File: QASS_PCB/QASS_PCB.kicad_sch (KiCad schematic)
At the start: 89 parts, among them U2 Seeeduino Xiao rp2040

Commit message: working on it
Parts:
- removed D1, D10, D11, D12, D13, D14, D15, D16, D17, D18, D19, D2, D20, D21, D22, D23, D24, D25, D26, D27, D28, D29, D3, D30, D31, D32, D33, D34, D35, D36, D37, D38, D39, D4, D5, D6, D7, D8, D9: D_Small, Diode_SMD:D_SOD-123, symbol Device:D_Small
- removed U2: Seeeduino Xiao rp2040, PCM_marbastlib-xp-promicroish:Xiao_rp2040_ACH, symbol PCM_marbastlib-promicroish:Seeeduino_Xiao_rp2040
- added D1, D10, D11, D12, D13, D14, D15, D16, D17, D18, D19, D2, D3, D4, D40, D5, D6, D7, D8, D9: BAV70_Small, Package_TO_SOT_SMD:SOT-23, symbol PCM_marbastlib-various:BAV70_Small
- added J1: Conn_01x02_Pin, Connector_PinHeader_2.54mm:PinHeader_1x02_P2.54mm_Vertical, symbol Connector:Conn_01x02_Pin
- added U1: ~, Einzelne Custom:Miao, symbol Miao:Miao_full_pinout
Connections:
- net c10 is gone; now on net c9: MX11.1
- net c1: now also MX13.2, MX2.2, MX23.2; no longer MX13.1, MX2.1, MX23.1
- net c2: now also MX33.2; no longer MX33.1
- net c3: now also MX15.2, MX25.2, MX4.2; no longer MX15.1, MX25.1, MX4.1
- net c4: now also MX35.2, MX40.2; no longer MX35.1, MX41.1
- net c5: now also MX17.2, MX27.2, MX41.1, MX6.2; no longer MX17.1, MX27.1, MX6.1
- net c6: now also MX37.2; no longer MX37.1, MX40.1
- net c7: now also MX19.2, MX29.2, MX8.2; no longer MX19.1, MX29.1, MX8.1
- net c8: now also MX39.2; no longer MX39.1
- net c9: now also MX10.2, MX21.2, MX31.2; no longer MX10.1, MX21.1, MX31.1
- net r0: now also D1.3 (K), D2.3 (K), D3.3 (K), D4.3 (K), D40.3 (K)
- net r1: now also D5.3 (K), D6.3 (K), D7.3 (K), D8.3 (K), D9.3 (K)
- net r2: now also D10.3 (K), D11.3 (K), D12.3 (K), D13.3 (K), D14.3 (K)
- net r3: now also D15.3 (K), D16.3 (K), D17.3 (K), D18.3 (K), D19.3 (K)
- net at MX14.2: now also D6.1 (A1)
- net at MX38.2: now also D18.1 (A1)
- net at MX30.2: now also D14.1 (A1)
- net at MX22.2: now also D10.1 (A1)
- net at MX41.2: now also MX36.2, MX42.2, D17.1 (A1); no longer MX35.2
- net at MX18.2: now also D8.1 (A1)
- net at MX28.2: now also D13.1 (A1)
- net at MX20.2: now also D9.1 (A1)
- net at MX7.2: now also D3.1 (A1)
- net at MX9.2: now also D4.1 (A1)
- net at MX24.2: now also D11.1 (A1)
- net at MX32.2: now also D15.1 (A1)
- net at MX26.2: now also D12.1 (A1)
- net at MX12.2: now also D5.1 (A1)
- net at MX16.2: now also D7.1 (A1)
- net at MX5.2: now also D2.1 (A1)
- net at MX11.2: now also D19.2 (A2)
- net at MX3.2: now also D1.1 (A1)
- net at MX1.2: now also D40.1 (A1)
- net at MX34.2: now also D16.1 (A1)
- new net: D7.2 (A2), MX17.1
- new net: D11.2 (A2), MX25.1
- new net: D40.2 (A2), MX2.1
- new net: D16.2 (A2), MX35.1, MX40.1
- new net: D4.2 (A2), MX10.1
- new net: D3.2 (A2), MX8.1
- new net: D18.2 (A2), MX39.1
- new net: D10.2 (A2), MX23.1
- new net: D5.2 (A2), MX13.1
- new net: D15.2 (A2), MX33.1
- new net: D6.2 (A2), MX15.1
- new net: D8.2 (A2), MX19.1
- new net: D17.2 (A2), MX37.1
- new net: D2.2 (A2), MX6.1
- new net: D1.2 (A2), MX4.1
- new net: D12.2 (A2), MX27.1
- new net: D13.2 (A2), MX29.1
- new net: D9.2 (A2), MX21.1
- new net: D14.2 (A2), MX31.1
- no-connect marks 0 -> 2
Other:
- note added: "L_Mods"
- note added: "R_Mods"
- note added: "Spacebars 2u"
- note added: "Spacebars 3u"
- note added: "Spacebars long"
- note added: "Xiao-compatibility for pads on backside"
- moved on the sheet: MX1, MX10, MX11, MX12, MX13, MX14, MX15, MX16, MX17, MX18, MX19, MX2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

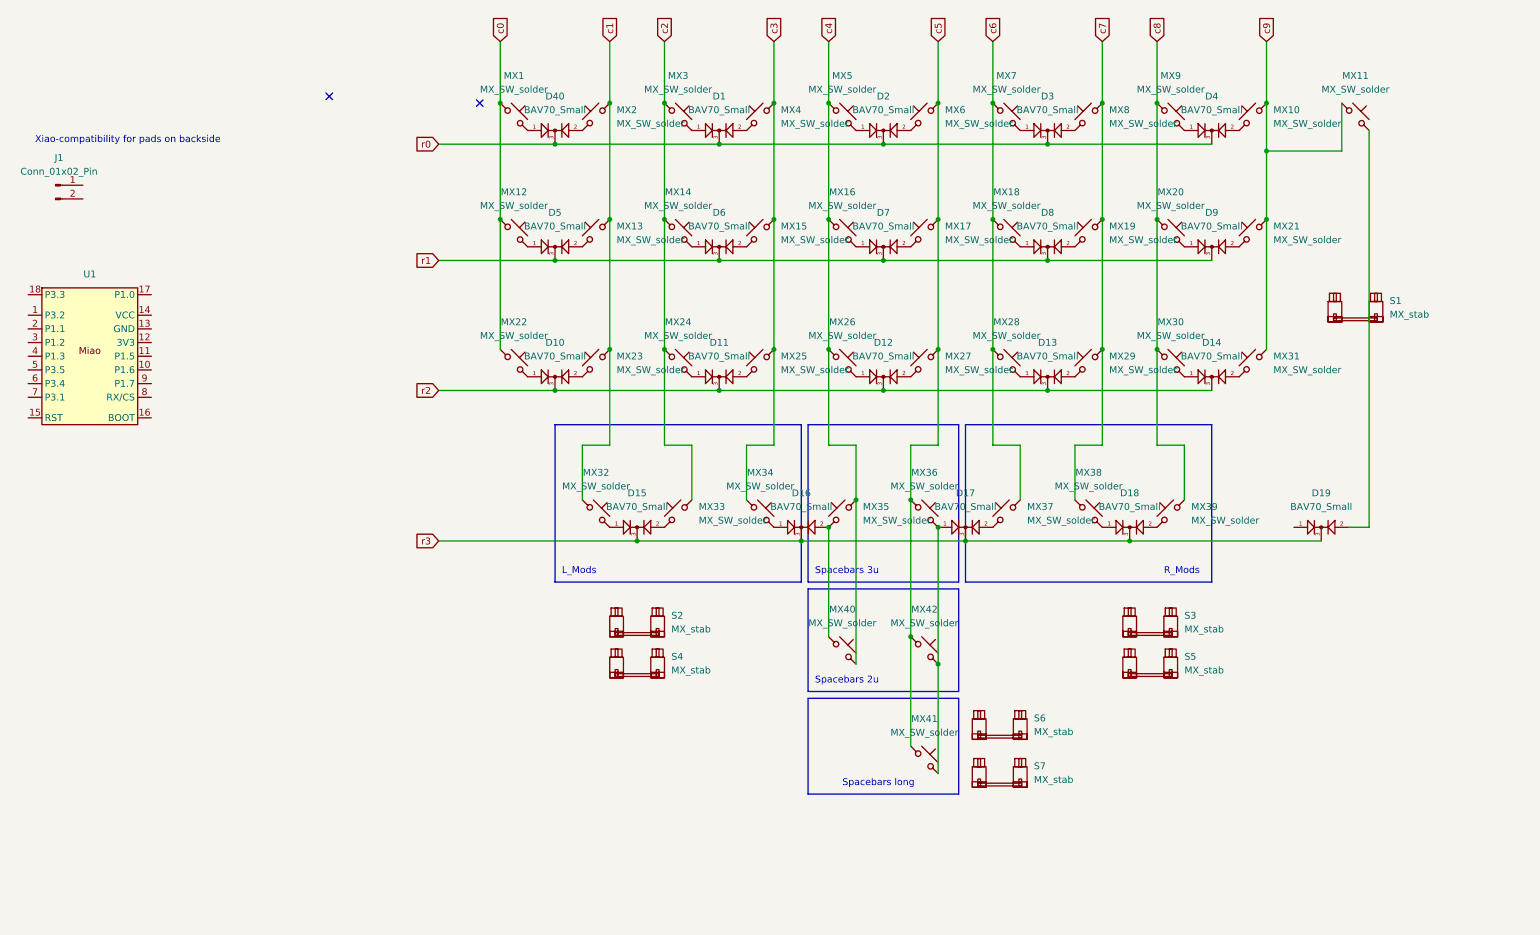
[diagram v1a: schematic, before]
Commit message: Routing down, pretty close to final
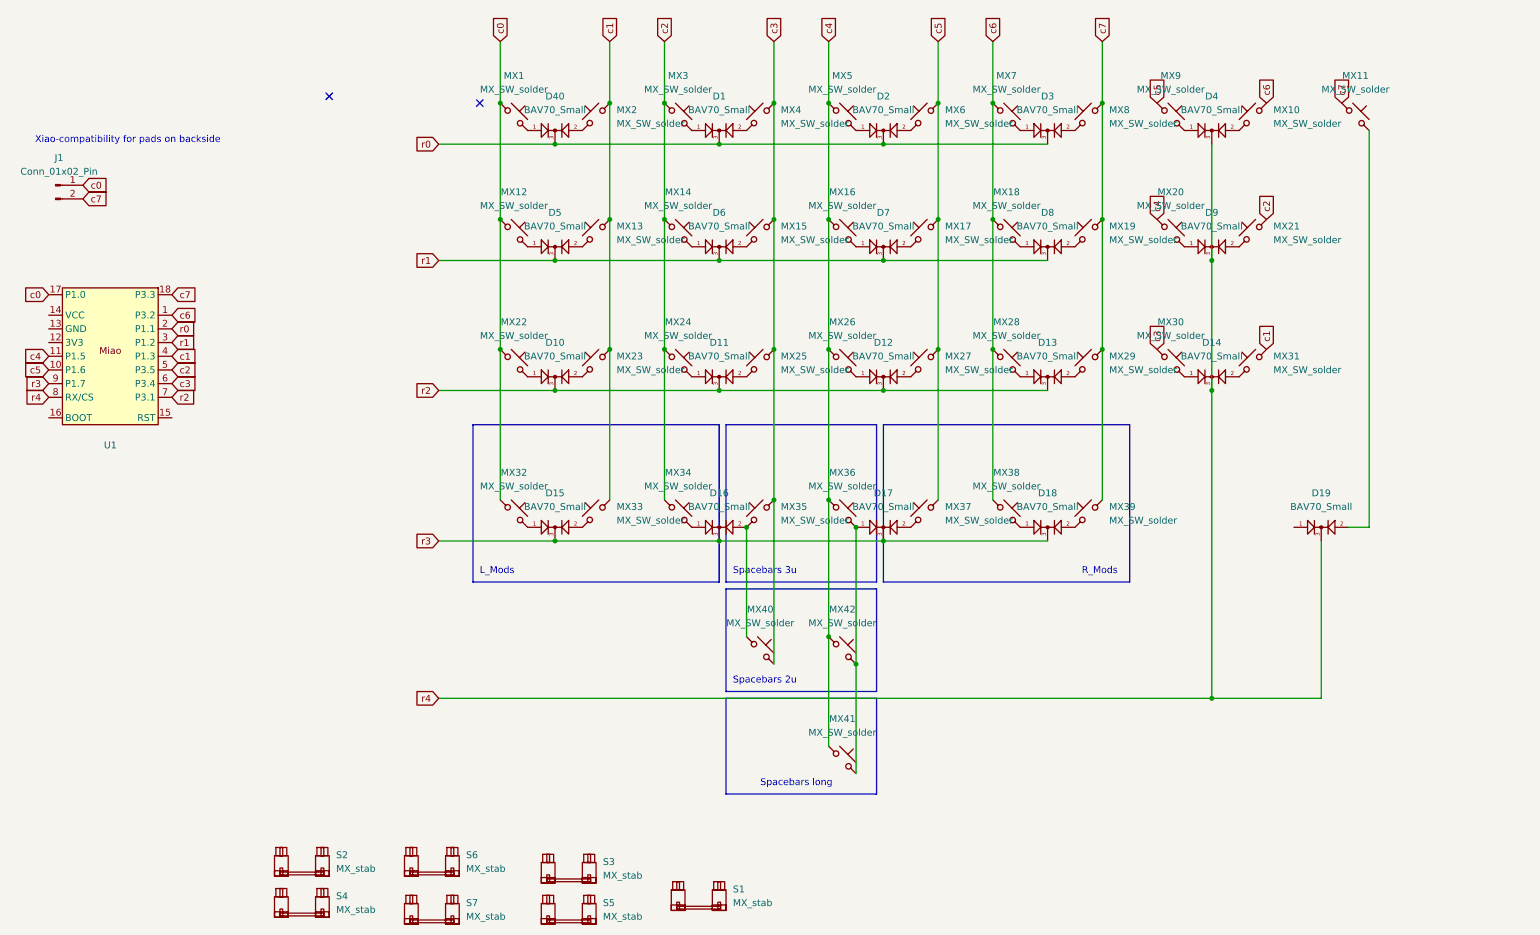
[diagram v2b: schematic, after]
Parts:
- S7: footprint PCM_marbastlib-mx:STAB_MX_P_7u -> PCM_marbastlib-mx:STAB_MX_P_10u
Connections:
- net c0: now also J1.1 (Pin_1), MX32.1, U1.17 (P1.0)
- net c1: now also MX31.2, MX33.2, U1.4 (P1.3); no longer MX32.1
- net c2: now also MX21.2, MX34.1, U1.5 (P3.5); no longer MX33.2
- net c3: now also MX30.1, MX35.2, MX40.2, U1.6 (P3.4); no longer MX34.1
- net c4: now also MX20.1, MX36.1, MX41.1, MX42.1, U1.11 (P1.5); no longer MX35.2, MX40.2
- net c5: now also MX37.2, MX9.1, U1.10 (P1.6); no longer MX36.1, MX41.1, MX42.1
- net c6: now also MX10.2, MX38.1, U1.1 (P3.2); no longer MX37.2
- net c7: now also J1.2 (Pin_2), MX11.1, MX39.2, U1.18 (P3.3); no longer MX38.1
- net r0: now also U1.2 (P1.1); no longer D4.3 (K)
- net r1: now also U1.3 (P1.2); no longer D9.3 (K)
- net r2: now also U1.7 (P3.1); no longer D14.3 (K)
- net r3: now also U1.9 (P1.7); no longer D19.3 (K)
- net r4: now reaches U1.8 (RX/CS)
- net r4: now also D14.3 (K), D19.3 (K), D4.3 (K), D9.3 (K)
- removed net c8: MX20.1, MX30.1, MX39.2, MX9.1
- removed net c9: MX10.2, MX11.1, MX21.2, MX31.2
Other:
- moved on the sheet: D15, D16, D17, D18, MX32, MX33, MX34, MX35, MX36, MX37, MX38, MX39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

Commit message: v1
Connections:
- no-connect marks 2 -> 6
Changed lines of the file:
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@@
 	)
 	(no_connect
-		(at 81.28 34.29)
+		(at 29.21 93.98)
 	)
 	(no_connect
-		(at 109.22 35.56)
+		(at 29.21 74.93)
+	)
+	(no_connect
+		(at 29.21 77.47)
+	)
+	(no_connect
+		(at 29.21 80.01)
+	)
+	(no_connect
+		(at 52.07 93.98)
+	)
+	(no_connect
+		(at 260.35 114.3)
 	)
 	(wire

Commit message: Added 2.75u right shift option
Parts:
- added MX43: MX_SW_solder, PCM_marbastlib-mx:SW_MX_1u, symbol PCM_marbastlib-mx:MX_SW_solder
- added S8: MX_stab, PCM_marbastlib-mx:STAB_MX_2.75u, symbol PCM_marbastlib-mx:MX_stab
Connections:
- net c1: now also MX43.2
- net at D14.2 (A2), MX31.1: now also MX43.1
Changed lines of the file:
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@@
 	)
 	(junction
+		(at 250.19 86.36)
+		(diameter 0)
+		(color 0 0 0 0)
+	)
+	(junction
 		(at 179.07 139.7)
 		(diameter 0)
@@
 	(wire
 		(pts
+			(xy 250.19 86.36) (xy 250.19 96.52)
+		)
+		(stroke
+			(width 0)
+			(type default)
+		)
+	)
+	(wire
+		(pts
 			(xy 163.83 109.22) (xy 163.83 139.7)
 		)
@@
 	(wire
 		(pts
+			(xy 255.27 81.28) (xy 255.27 91.44)
+		)
+		(stroke
+			(width 0)
+			(type default)
+		)
+	)
+	(wire
+		(pts
 			(xy 245.11 43.18) (xy 245.11 64.77)
 		)
@@
 	)
 	(symbol
+		(lib_id "PCM_marbastlib-mx:MX_SW_solder")
+		(at 252.73 93.98 90)
+		(unit 1)
+		(exclude_from_sim no)
+		(in_bom yes)
+		(on_board yes)
+		(dnp no)
+		(fields_autoplaced yes)
+		(property "Reference" "MX43"
+			(at 256.54 92.71 90)
+			(effects
+				(font
+					(size 1.27 1.27)
+				)
+				(justify right)
+			)
+		)
+		(property "Value" "MX_SW_solder"
+			(at 256.54 95.25 90)
+			(effects
+				(font
+					(size 1.27 1.27)
+				)
+				(justify right)
+			)
+		)
+		(property "Footprint" "PCM_marbastlib-mx:SW_MX_1u"
+			(at 252.73 93.98 0)
+			(effects
+				(font
+					(size 1.27 1.27)
+				)
+				(hide yes)
+			)
+		)
+		(property "Datasheet" "~"
+			(at 252.73 93.98 0)
+			(effects
+				(font
+					(size 1.27 1.27)
+				)
+				(hide yes)
+			)
+		)
+		(property "Description" ""
+			(at 252.73 93.98 0)
+			(effects
+				(font
+					(size 1.27 1.27)
+				)
+				(hide yes)
+			)
+		)
+		(pin "2"
+		)
+		(pin "1"
+		)
+		(instances
+			(project "QASS_PCB"
+				(path "/4e836cba-8d9e-4ad4-ae4d-2f7aa930d50f"
+					(reference "MX43")
+					(unit 1)
+				)
+			)
+		)
+	)
+	(symbol
 		(lib_id "PCM_marbastlib-various:BAV70_Small")
 		(at 123.19 40.64 0)
@@
 					(unit 1)
 				)
+			)
+		)
+	)
+	(symbol
+		(lib_id "PCM_marbastlib-mx:MX_stab")
+		(at 153.67 171.45 0)
+		(unit 1)
+		(exclude_from_sim no)
+		(in_bom yes)
+		(on_board yes)
+		(dnp no)
+		(fields_autoplaced yes)
+		(property "Reference" "S8"
+			(at 160.02 170.053 0)
+			(effects
+				(font
+					(size 1.27 1.27)
+				)
+				(justify left)
+			)
+		)
+		(property "Value" "MX_stab"
+			(at 160.02 172.593 0)
+			(effects
+				(font
+					(size 1.27 1.27)
+				)
+				(justify left)
+			)
+		)
+		(property "Footprint" "PCM_marbastlib-mx:STAB_MX_2.75u"
+			(at 153.67 171.45 0)
+			(effects
+				(font
+					(size 1.27 1.27)
+				)
+				(hide yes)
+			)
+		)
+		(property "Datasheet" ""
+			(at 153.67 171.45 0)
+			(effects
+				(font
+					(size 1.27 1.27)
+				)
+				(hide yes)
+			)
+		)
+		(property "Description" ""
+			(at 153.67 171.45 0)
+			(effects
+				(font
+					(size 1.27 1.27)
+				)
+				(hide yes)
+			)
+		)
+		(instances
+			(project "QASS_PCB"
+				(path "/4e836cba-8d9e-4ad4-ae4d-2f7aa930d50f"
+					(reference "S8")
+					(unit 1)
+				)

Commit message: Added ISO Enter
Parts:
- added MX44: MX_SW_solder, PCM_marbastlib-mx:SW_MX_1.5u, symbol PCM_marbastlib-mx:MX_SW_solder
- added MX45: MX_SW_solder, PCM_marbastlib-mx:SW_MX_1u, symbol PCM_marbastlib-mx:MX_SW_solder
- added S9: MX_stab, PCM_marbastlib-mx:STAB_MX_P_ISO, symbol PCM_marbastlib-mx:MX_stab
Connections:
- net c2: now also MX45.2
- net c7: now also MX44.1
- net at D19.2 (A2), MX11.2: now also MX44.2
- net at D9.2 (A2), MX21.1: now also MX45.1
